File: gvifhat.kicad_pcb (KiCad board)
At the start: 2 copper layers, 85.3 x 56.4 mm, 66 parts, among them J1 Raspberry_Pi_2_3, J2 GVIFout, J3 GVIFin, J4 USB_A, J5 USB_A, J6 touch_IN, J7 touch_OUT, U1 CXB1457R, U2 PCF8563TS, U3 4066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

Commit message: small PCB layout update
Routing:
- net Net-(J3-Pin_2): track 42.8 -> 21.5 mm, vias 0 -> 2
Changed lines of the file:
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@@
   (segment (start 101.505 89.65) (end 99.65 88.785) (width 0.25) (layer "F.Cu") (net 34))
   (segment (start 109.124 93.278) (end 108.8512 92.3584) (width 0.25) (layer "F.Cu") (net 34))
-  (segment (start 115.8577 84.9513) (end 101.6561 75.5199) (width 0.25) (layer "F.Cu") (net 35))
-  (segment (start 116.744 86.353) (end 116.5119 85.3927) (width 0.25) (layer "F.Cu") (net 35))
-  (segment (start 97.2449 89.9511) (end 98.66 93.785) (width 0.25) (layer "F.Cu") (net 35))
-  (segment (start 116.4994 85.3803) (end 115.9066 84.9839) (width 0.25) (layer "F.Cu") (net 35))
-  (segment (start 101.6561 75.5199) (end 97.6961 75.5199) (width 0.25) (layer "F.Cu") (net 35))
-  (segment (start 97.0949 78.1011) (end 97.0949 82.4921) (width 0.25) (layer "F.Cu") (net 35))
-  (segment (start 97.0949 77.7489) (end 97.0949 78.1011) (width 0.25) (layer "F.Cu") (net 35))
-  (segment (start 97.0949 82.4921) (end 97.2449 89.9511) (width 0.25) (layer "F.Cu") (net 35))
-  (segment (start 98.66 93.785) (end 99.65 93.785) (width 0.25) (layer "F.Cu") (net 35))
-  (segment (start 115.9066 84.9839) (end 115.8577 84.9513) (width 0.25) (layer "F.Cu") (net 35))
-  (segment (start 97.0949 75.7689) (end 97.0949 77.7489) (width 0.25) (layer "F.Cu") (net 35))
-  (segment (start 116.5119 85.3927) (end 116.4994 85.3803) (width 0.25) (layer "F.Cu") (net 35))
-  (segment (start 97.6961 75.5199) (end 97.3439 75.5199) (width 0.25) (layer "F.Cu") (net 35))
-  (segment (start 97.3439 75.5199) (end 97.0949 75.7689) (width 0.25) (layer "F.Cu") (net 35))
+  (segment (start 116.744 88.344) (end 116.8 88.4) (width 0.25) (layer "F.Cu") (net 35))
+  (segment (start 102.585 93.785) (end 102.6 93.8) (width 0.25) (layer "F.Cu") (net 35))
+  (segment (start 116.744 86.353) (end 116.744 88.344) (width 0.25) (layer "F.Cu") (net 35))
+  (segment (start 99.65 93.785) (end 102.585 93.785) (width 0.25) (layer "F.Cu") (net 35))
+  (via (at 102.6 93.8) (size 0.8) (drill 0.4) (layers "F.Cu" "B.Cu") (net 35))
+  (via (at 116.8 88.4) (size 0.8) (drill 0.4) (layers "F.Cu" "B.Cu") (net 35))
+  (segment (start 113.075 88.525) (end 107.8 93.8) (width 0.25) (layer "B.Cu") (net 35))
+  (segment (start 116.8 88.4) (end 116.675 88.525) (width 0.25) (layer "B.Cu") (net 35))
+  (segment (start 116.675 88.525) (end 113.075 88.525) (width 0.25) (layer "B.Cu") (net 35))
+  (segment (start 107.8 93.8) (end 102.6 93.8) (width 0.25) (layer "B.Cu") (net 35))
   (segment (start 129.654 102.6) (end 126.5168 102.8669) (width 0.25) (layer "F.Cu") (net 36))
   (segment (start 126.5168 102.8669) (end 126.05 103.1625) (width 0.25) (layer "F.Cu") (net 36))

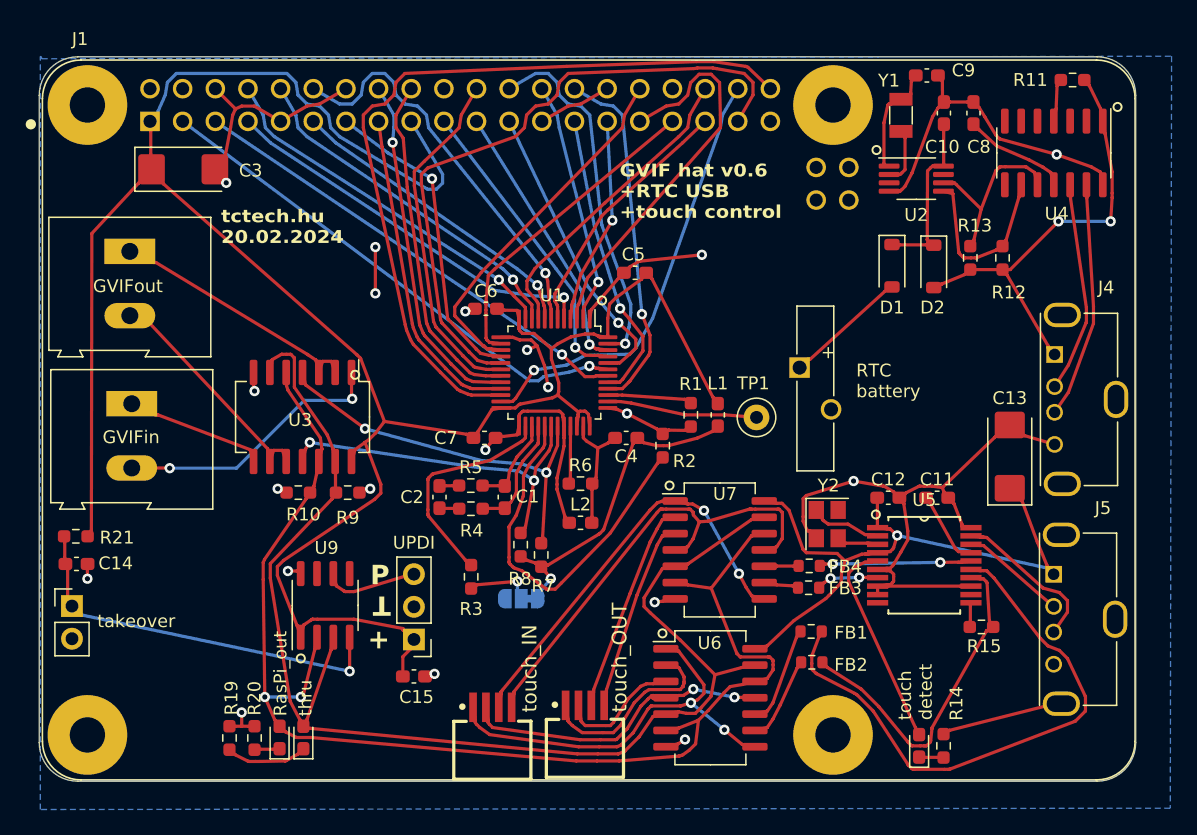
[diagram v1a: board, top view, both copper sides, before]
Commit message: replaced solder-in battery with a cr1220 holder
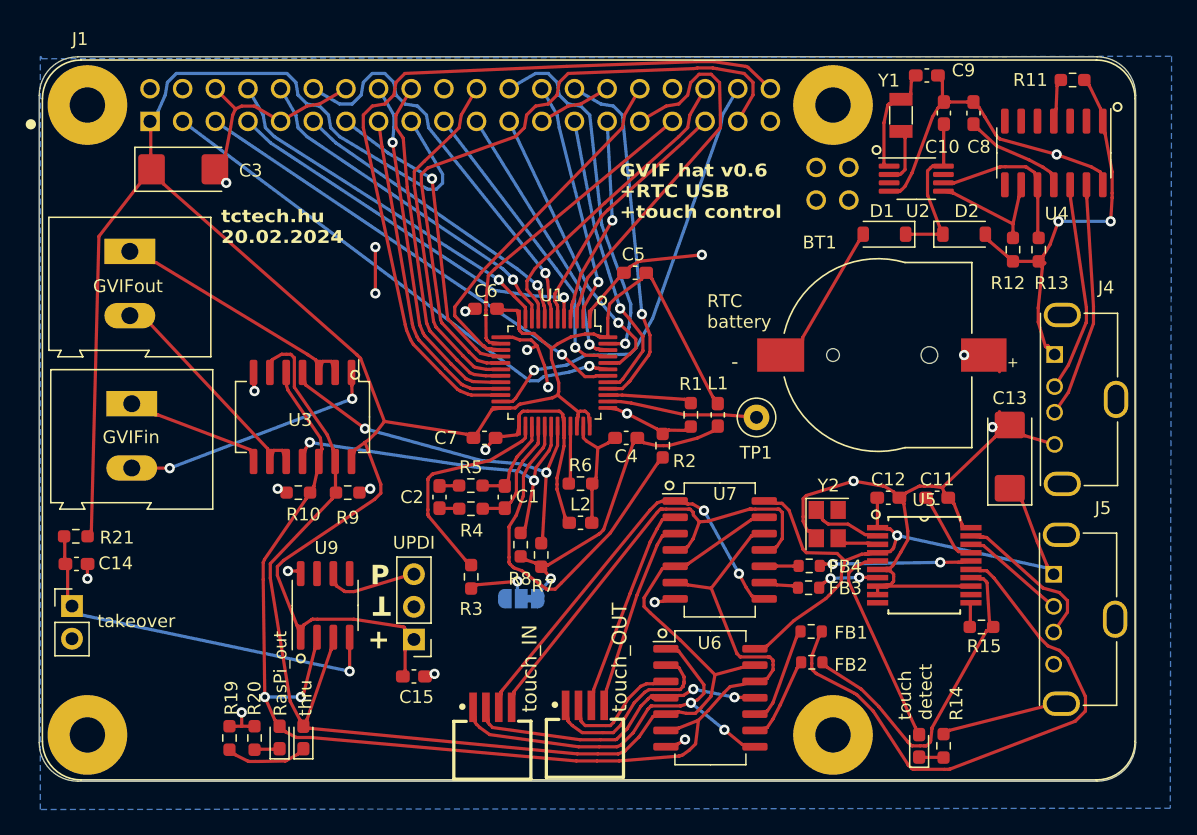
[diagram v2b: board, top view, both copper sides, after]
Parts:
- BT1: footprint Battery:Battery_Panasonic_CR1220-VCN_Vertical_CircularHoles -> hdmi2lvds:MPD_BC501SM-TR
- moved BT1 6.18 mm to (157.7, 85.0), turned to 0 degrees
- moved R13 5.36 mm to (170.2, 76.8)
- moved D2 3.44 mm to (164.4, 75.6), turned to 0 degrees
- moved D1 2.52 mm to (158.2, 75.6), turned to 180 degrees
- moved R12 1.03 mm to (168.2, 76.8)
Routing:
- net Net-(U2-SDA): track 14.1 -> 10.2 mm
- net GND: track 164.8 -> 167.8 mm, vias 20 -> 22
- net Net-(BT1-+): track 9.60 -> 11.6 mm
- net Net-(U2-SCL): track 14.2 -> 12.6 mm
- net USBvdd: track 34.9 -> 33.6 mm
- net Net-(J3-Pin_2): track 21.5 -> 20.2 mm
- net Net-(D1-K): track 13.9 -> 12.7 mm
